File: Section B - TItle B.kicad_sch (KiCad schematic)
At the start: 0 parts

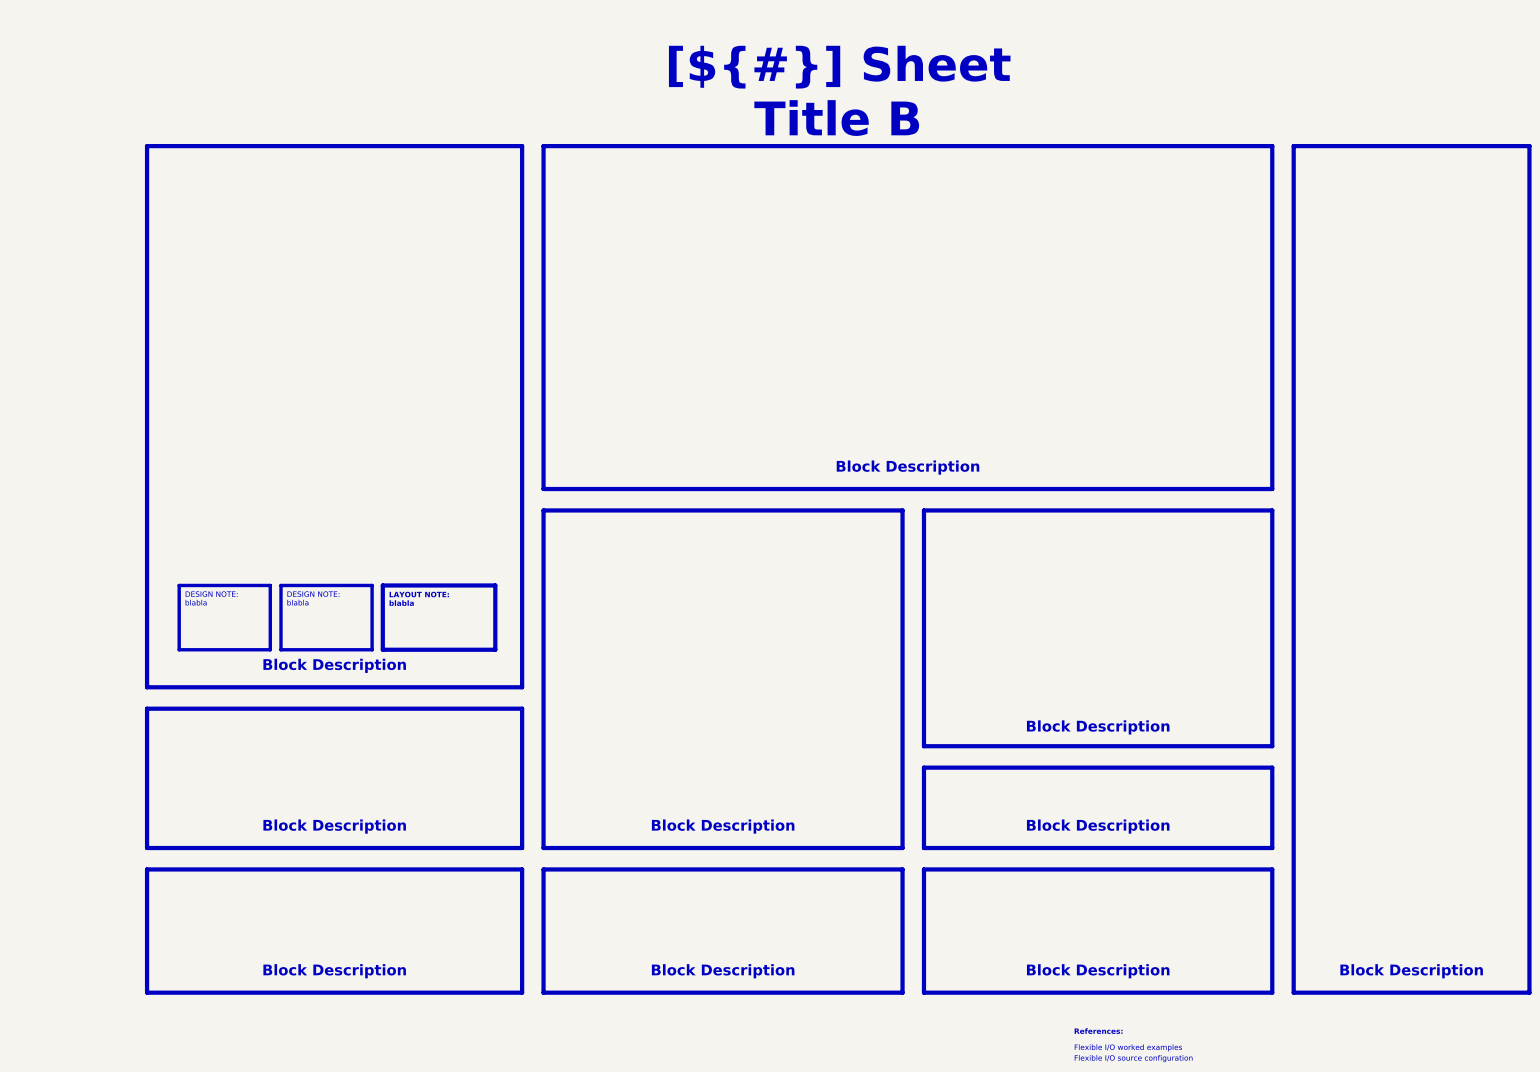
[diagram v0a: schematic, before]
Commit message: CM5 IO done
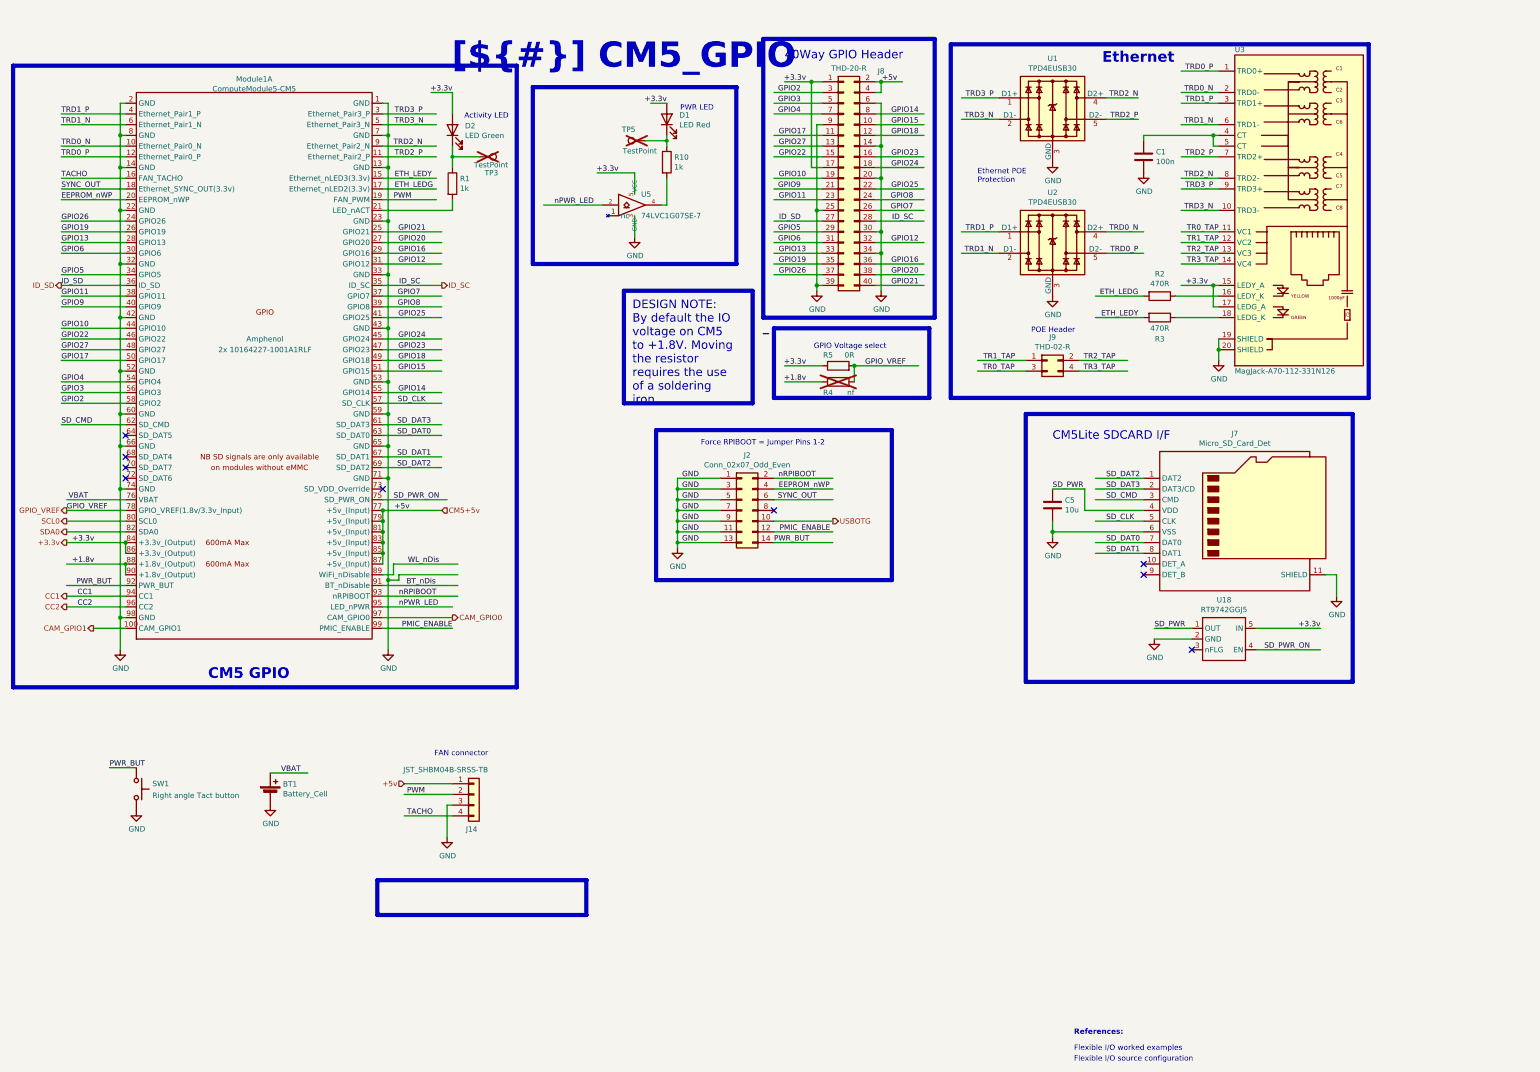
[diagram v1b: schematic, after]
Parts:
- added BT1: Battery_Cell, CM5IO:BatteryHolder_Keystone_3034_1x20mm, symbol Device:Battery_Cell
- added C1: 100n, Capacitor_SMD:C_0402_1005Metric, symbol Device:C
- added C5: 10u, Capacitor_SMD:C_0805_2012Metric, symbol Device:C
- added D1: LED Red, LED_SMD:LED_0603_1608Metric, symbol Device:LED
- added D2: LED Green, LED_SMD:LED_0603_1608Metric, symbol Device:LED
- added J14: JST_SHBM04B-SRSS-TB, Connector_JST:JST_SH_BM04B-SRSS-TB_1x04-1MP_P1.00mm_Vertical, symbol Connector_Generic:Conn_01x04
- added J2: Conn_02x07_Odd_Even, Connector_PinHeader_2.54mm:PinHeader_2x07_P2.54mm_Vertical, symbol Connector_Generic:Conn_02x07_Odd_Even
- added J7: Micro_SD_Card_Det, CM5IO:SDCARD_MOLEX_503398-1892, symbol Connector:Micro_SD_Card_Det2
- added J8: THD-20-R, Connector_PinHeader_2.54mm:PinHeader_2x20_P2.54mm_Vertical, symbol Connector_Generic:Conn_02x20_Odd_Even
- added J9: THD-02-R, Connector_PinHeader_2.54mm:PinHeader_2x02_P2.54mm_Vertical, symbol Connector_Generic:Conn_02x02_Odd_Even
- added Module1: ComputeModule5-CM5, CM5IO:Raspberry-Pi-5-Compute-Module, symbol CM5IO:ComputeModule5-CM5
- added R1, R10: 1k, Resistor_SMD:R_0402_1005Metric, symbol Device:R
- added R2, R3: 470R, Resistor_SMD:R_0402_1005Metric, symbol Device:R
- added R4: nf, Resistor_SMD:R_0805_2012Metric_Pad1.20x1.40mm_HandSolder, symbol Device:R
- added R5: 0R, Resistor_SMD:R_0805_2012Metric_Pad1.20x1.40mm_HandSolder, symbol Device:R
- added SW1: Right angle Tact button, Button_Switch_THT:SW_Tactile_SPST_Angled_PTS645Vx58-2LFS, symbol Switch:SW_Push
- added TP3, TP5: TestPoint, TestPoint:TestPoint_Pad_2.0x2.0mm, symbol Connector:TestPoint
- added U1, U2: TPD4EUSB30, Package_SON:USON-10_2.5x1.0mm_P0.5mm, symbol CM5IO:TPD4EUSB30
- added U18: RT9742GGJ5, Package_TO_SOT_SMD:SOT-23-5, symbol CM5IO:RT9742GGJ5
- added U3: MagJack-A70-112-331N126, CM5IO:TRJG0926HENL, symbol CM5IO:MagJack-A70-112-331N126
- added U5: 74LVC1G07SE-7, Package_TO_SOT_SMD:SOT-353_SC-70-5, symbol CM5IO:74LVC1G07_copy
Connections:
- new net: R10.2, U5.4
- new net: C1.1, U3.4 (CT), U3.5 (CT)
- new net: R2.1, U3.16 (LEDY_K)
- new net: R3.1, U3.18 (LEDG_K)
- new net: D2.1 (K), R1.1, TP3.1
- new net: Module1.21 (LED_nACT), R1.2
- new net: D1.1 (K), R10.1, TP5.1
- new net +1.8v: Module1.88 (+1.8v_(Output)), Module1.90 (+1.8v_(Output)), R4.1
- new net +3.3v: D1.2 (A), D2.2 (A), J8.1 (Pin_1), J8.17 (Pin_17), Module1.84 (+3.3v_(Output)), Module1.86 (+3.3v_(Output)), R5.1, U18.5 (IN), U3.15 (LEDY_A), U3.17 (LEDG_A), U5.5 (VCC)
- new net +5v: J14.1 (Pin_1), J8.2 (Pin_2), J8.4 (Pin_4), Module1.77 (+5v_(Input)), Module1.79 (+5v_(Input)), Module1.81 (+5v_(Input)), Module1.83 (+5v_(Input)), Module1.85 (+5v_(Input)), Module1.87 (+5v_(Input))
- new net BT_nDis: Module1.91 (BT_nDisable)
- new net CAM_GPIO0: Module1.97 (CAM_GPIO0)
- new net CAM_GPIO1: Module1.100 (CAM_GPIO1)
- new net CC1: Module1.94 (CC1)
- new net CC2: Module1.96 (CC2)
- new net EEPROM_nWP: J2.4 (Pin_4), Module1.20 (EEPROM_nWP)
- new net ETH_LEDG: Module1.17 (Ethernet_nLED2(3.3v)), R2.2
- new net ETH_LEDY: Module1.15 (Ethernet_nLED3(3.3v)), R3.2
- new net GND: BT1.2 (-), C1.2, C5.2, J14.3 (Pin_3), J2.1 (Pin_1), J2.11 (Pin_11), J2.13 (Pin_13), J2.3 (Pin_3), J2.5 (Pin_5), J2.7 (Pin_7), J2.9 (Pin_9), J7.11 (SHIELD), J7.6 (VSS), J8.14 (Pin_14), J8.20 (Pin_20), J8.25 (Pin_25), J8.30 (Pin_30), J8.34 (Pin_34), J8.39 (Pin_39), J8.6 (Pin_6), J8.9 (Pin_9), Module1.1 (GND), Module1.13 (GND), Module1.14 (GND), Module1.2 (GND), Module1.22 (GND), Module1.23 (GND), Module1.32 (GND), Module1.33 (GND), Module1.42 (GND), Module1.43 (GND), Module1.52 (GND), Module1.53 (GND), Module1.59 (GND), Module1.60 (GND), Module1.65 (GND), Module1.66 (GND), Module1.7 (GND), Module1.71 (GND), Module1.74 (GND), Module1.8 (GND), Module1.98 (GND), SW1.2, U1.3 (GND), U1.8 (GND), U18.2 (GND), U2.3 (GND), U2.8 (GND), U3.19 (SHIELD), U3.20 (SHIELD), U5.3 (GND)
- new net GPIO10: J8.19 (Pin_19), Module1.44 (GPIO10)
- new net GPIO11: J8.23 (Pin_23), Module1.38 (GPIO11)
- new net GPIO12: J8.32 (Pin_32), Module1.31 (GPIO12)
- new net GPIO13: J8.33 (Pin_33), Module1.28 (GPIO13)
- new net GPIO14: J8.8 (Pin_8), Module1.55 (GPIO14)
- new net GPIO15: J8.10 (Pin_10), Module1.51 (GPIO15)
- new net GPIO16: J8.36 (Pin_36), Module1.29 (GPIO16)
- new net GPIO17: J8.11 (Pin_11), Module1.50 (GPIO17)
- new net GPIO18: J8.12 (Pin_12), Module1.49 (GPIO18)
- new net GPIO19: J8.35 (Pin_35), Module1.26 (GPIO19)
- new net GPIO2: J8.3 (Pin_3), Module1.58 (GPIO2)
- new net GPIO20: J8.38 (Pin_38), Module1.27 (GPIO20)
- new net GPIO21: J8.40 (Pin_40), Module1.25 (GPIO21)
- new net GPIO22: J8.15 (Pin_15), Module1.46 (GPIO22)
- new net GPIO23: J8.16 (Pin_16), Module1.47 (GPIO23)
- new net GPIO24: J8.18 (Pin_18), Module1.45 (GPIO24)
- new net GPIO25: J8.22 (Pin_22), Module1.41 (GPIO25)
- new net GPIO26: J8.37 (Pin_37), Module1.24 (GPIO26)
- new net GPIO27: J8.13 (Pin_13), Module1.48 (GPIO27)
- new net GPIO3: J8.5 (Pin_5), Module1.56 (GPIO3)
- new net GPIO4: J8.7 (Pin_7), Module1.54 (GPIO4)
- new net GPIO5: J8.29 (Pin_29), Module1.34 (GPIO5)
- new net GPIO6: J8.31 (Pin_31), Module1.30 (GPIO6)
- new net GPIO7: J8.26 (Pin_26), Module1.37 (GPIO7)
- new net GPIO8: J8.24 (Pin_24), Module1.39 (GPIO8)
- new net GPIO9: J8.21 (Pin_21), Module1.40 (GPIO9)
- new net GPIO_VREF: Module1.78 (GPIO_VREF(1.8v/3.3v_Input)), R4.2, R5.2
- new net ID_SC: J8.28 (Pin_28), Module1.35 (ID_SC)
- new net ID_SD: J8.27 (Pin_27), Module1.36 (ID_SD)
- new net PMIC_ENABLE: J2.12 (Pin_12), Module1.99 (PMIC_ENABLE)
- new net PWM: J14.2 (Pin_2), Module1.19 (FAN_PWM)
- new net PWR_BUT: J2.14 (Pin_14), Module1.92 (PWR_BUT), SW1.1
- new net SCL0: Module1.80 (SCL0)
- new net SDA0: Module1.82 (SDA0)
- new net SD_CLK: J7.5 (CLK), Module1.57 (SD_CLK)
- new net SD_CMD: J7.3 (CMD), Module1.62 (SD_CMD)
- new net SD_DAT0: J7.7 (DAT0), Module1.63 (SD_DAT0)
- new net SD_DAT1: J7.8 (DAT1), Module1.67 (SD_DAT1)
- new net SD_DAT2: J7.1 (DAT2), Module1.69 (SD_DAT2)
- new net SD_DAT3: J7.2 (DAT3/CD), Module1.61 (SD_DAT3)
- new net SD_PWR: C5.1, J7.4 (VDD), U18.1 (OUT)
- new net SD_PWR_ON: Module1.75 (SD_PWR_ON), U18.4 (EN)
- new net SYNC_OUT: J2.6 (Pin_6), Module1.18 (Ethernet_SYNC_OUT(3.3v))
- new net TACHO: J14.4 (Pin_4), Module1.16 (FAN_TACHO)
- new net TR0_TAP: J9.3 (Pin_3), U3.11 (VC1)
- new net TR1_TAP: J9.1 (Pin_1), U3.12 (VC2)
- new net TR2_TAP: J9.2 (Pin_2), U3.13 (VC3)
- new net TR3_TAP: J9.4 (Pin_4), U3.14 (VC4)
- new net TRD0_N: Module1.10 (Ethernet_Pair0_N), U2.4 (D2+), U2.7, U3.2 (TRD0-)
- new net TRD0_P: Module1.12 (Ethernet_Pair0_P), U2.5 (D2-), U2.6, U3.1 (TRD0+)
- new net TRD1_N: Module1.6 (Ethernet_Pair1_N), U2.2 (D1-), U2.9, U3.6 (TRD1-)
- new net TRD1_P: Module1.4 (Ethernet_Pair1_P), U2.1 (D1+), U2.10, U3.3 (TRD1+)
- new net TRD2_N: Module1.9 (Ethernet_Pair2_N), U1.4 (D2+), U1.7, U3.8 (TRD2-)
- new net TRD2_P: Module1.11 (Ethernet_Pair2_P), U1.5 (D2-), U1.6, U3.7 (TRD2+)
- new net TRD3_N: Module1.5 (Ethernet_Pair3_N), U1.2 (D1-), U1.9, U3.10 (TRD3-)
- new net TRD3_P: Module1.3 (Ethernet_Pair3_P), U1.1 (D1+), U1.10, U3.9 (TRD3+)
- new net USBOTG: J2.10 (Pin_10)
- new net VBAT: BT1.1 (+), Module1.76 (VBAT)
- new net WL_nDis: Module1.89 (WiFi_nDisable)
- new net nPWR_LED: Module1.95 (LED_nPWR), U5.2
- new net nRPIBOOT: J2.2 (Pin_2), Module1.93 (nRPIBOOT)
- no-connect marks 0 -> 9
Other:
- note added: "40Way GPIO Header"
- note added: "Activity LED"
- note added: "CM5Lite SDCARD I/F"
- note added: "Ethernet POE Protection"
- note added: "FAN connector"
- note added: "Force RPIBOOT = Jumper Pins 1-2"
- note added: "GPIO Voltage select"
- note added: "POE Header"
- note added: "PWR LED"
- title: Sheet Title B -> CM5_GPIO
